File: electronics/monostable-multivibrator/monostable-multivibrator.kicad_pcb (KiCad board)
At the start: 2 copper layers, 50.8 x 40.6 mm, 20 parts, among them J1 + PWR -, J2 - LOAD +, Q1 2N3904, SW1 NO CO NC, SW2 + -, U1 NE555P, U2 LM7805

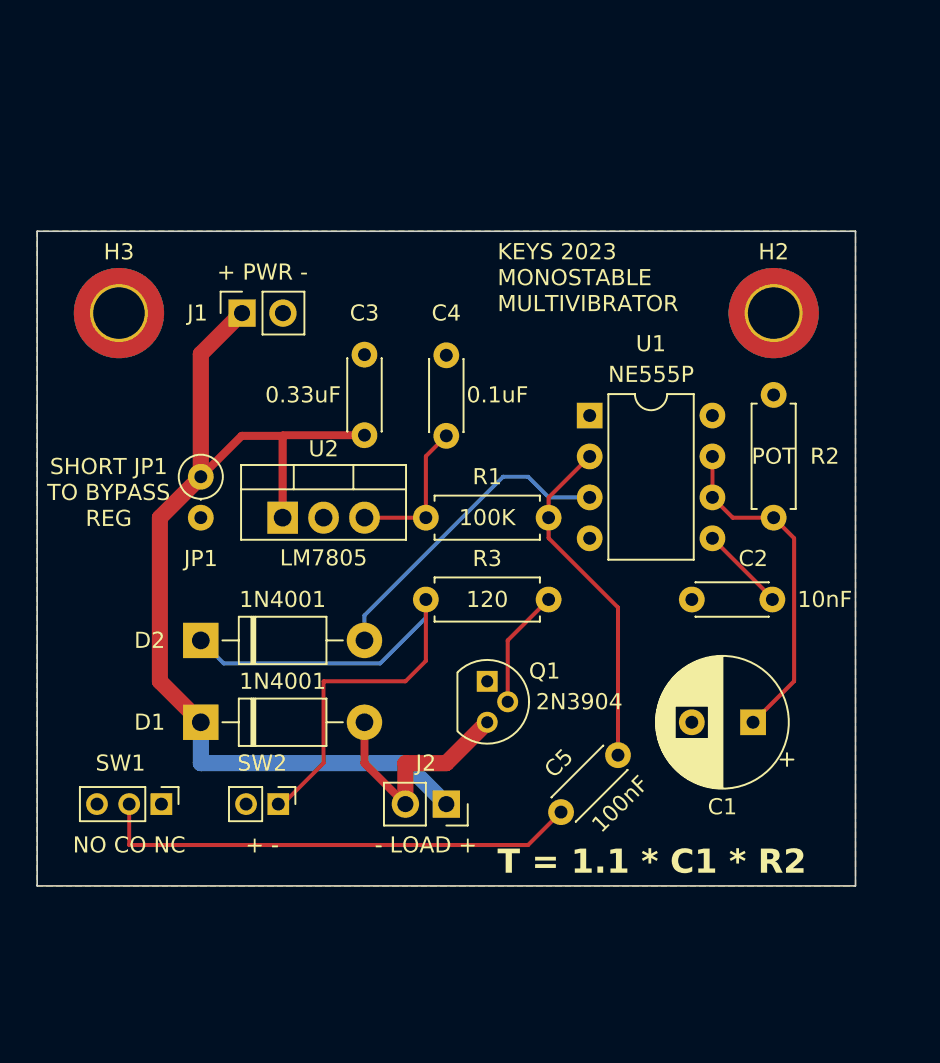
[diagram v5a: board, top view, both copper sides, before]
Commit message: fixing switch spacing, fixing 100nF to 0.1uF
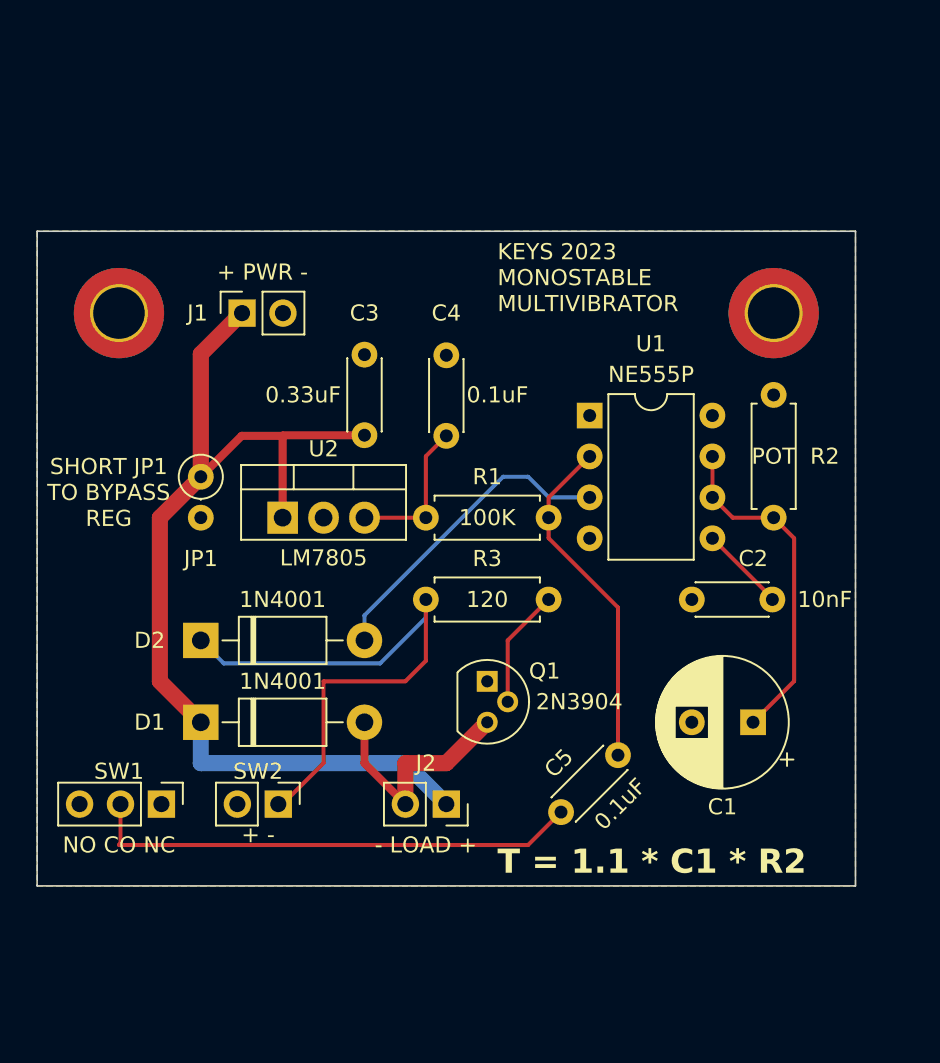
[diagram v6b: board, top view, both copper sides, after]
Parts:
- C5: value 100nF -> 0.1uF
- SW1: footprint Connector_PinHeader_2.00mm:PinHeader_1x03_P2.00mm_Vertical -> Connector_PinHeader_2.54mm:PinHeader_1x03_P2.54mm_Vertical
- SW2: footprint Connector_PinHeader_2.00mm:PinHeader_1x02_P2.00mm_Vertical -> Connector_PinHeader_2.54mm:PinHeader_1x02_P2.54mm_Vertical
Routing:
- net Net-(SW1-B): track 30.2 -> 30.9 mm
